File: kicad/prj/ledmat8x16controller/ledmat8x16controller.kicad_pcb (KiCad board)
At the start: 2 copper layers, 63.8 x 31.9 mm, 13 parts, among them J1 Conn_02x08_Odd_Even, J2 Conn_01x02, J3 Conn_01x02_Pin, J4 Conn_01x02_Pin, J6 Conn_01x02_Pin, J8 Conn_01x09_Pin, SW2 SW_Push

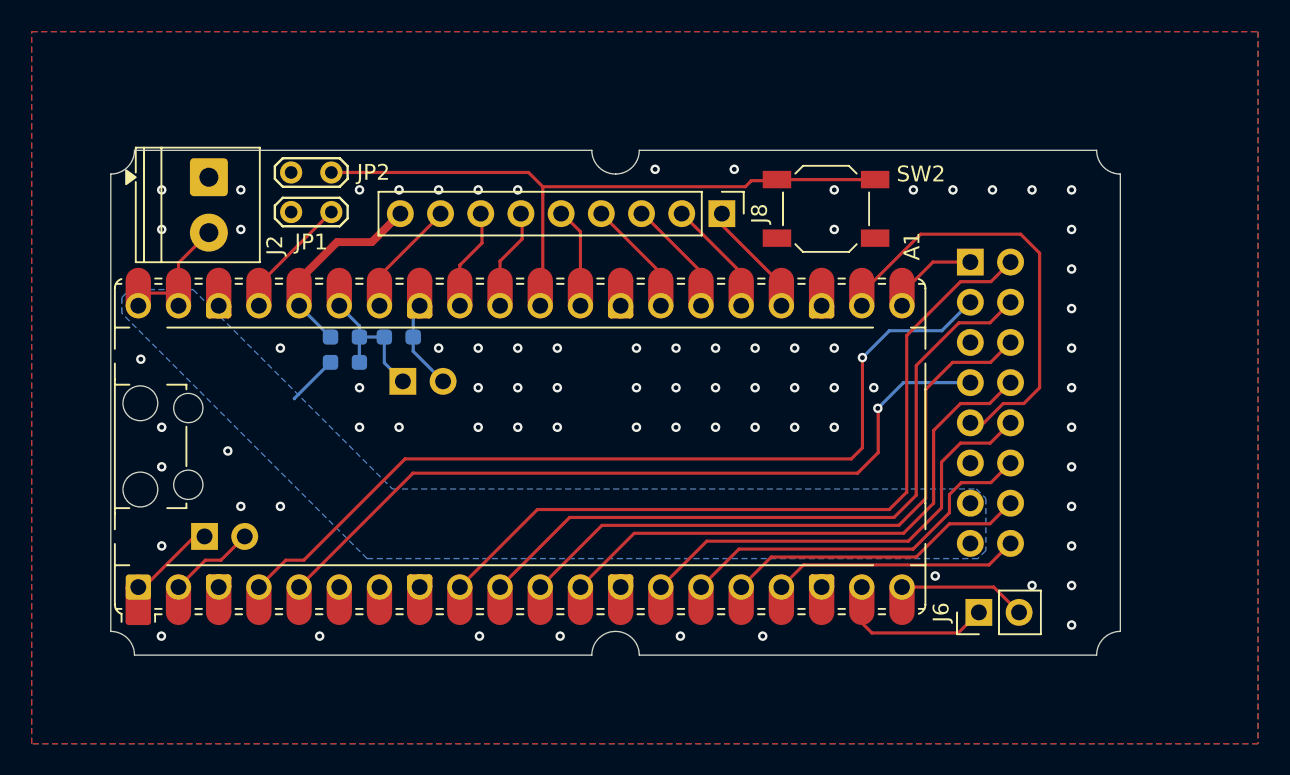
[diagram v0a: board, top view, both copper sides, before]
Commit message: Resize controller board to 32mm outline
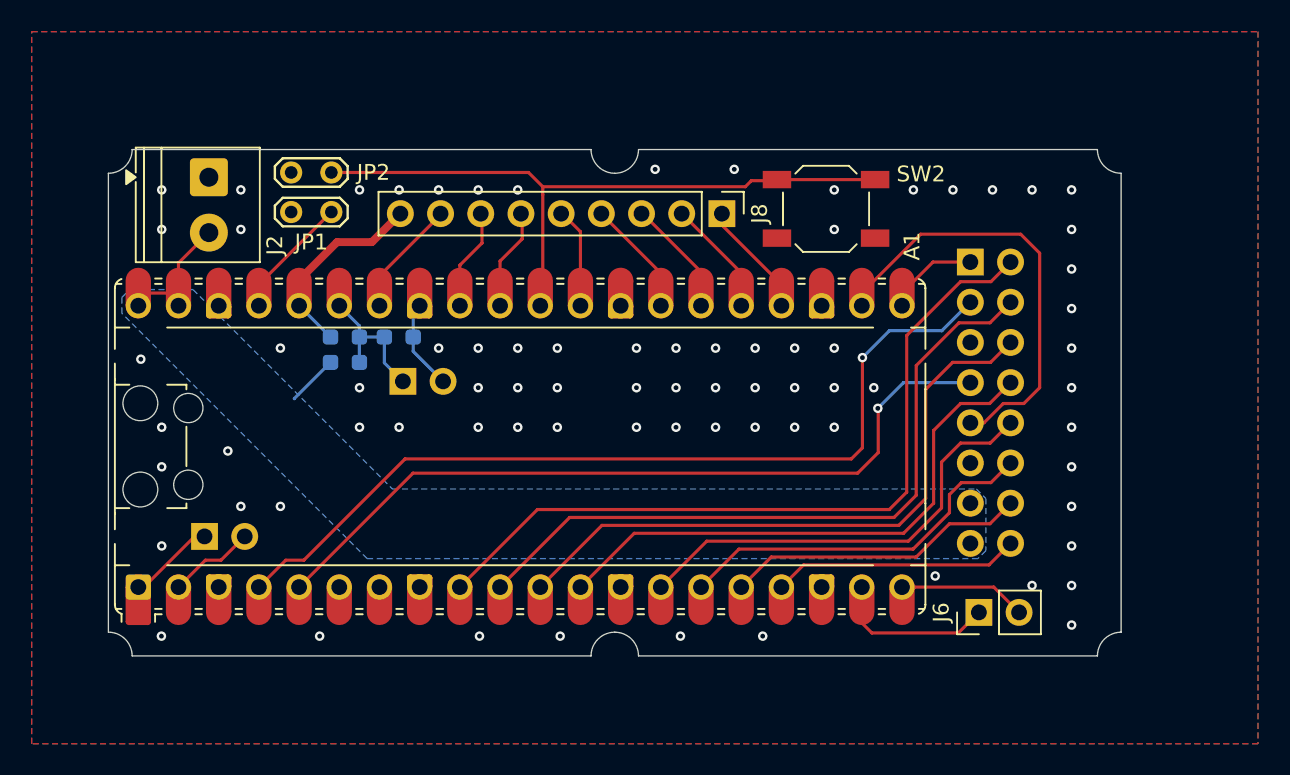
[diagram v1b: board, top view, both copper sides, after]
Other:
- board size 63.8 x 31.9 mm -> 64 x 32 mm
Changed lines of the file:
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@@
 		)
 	)
+	(property "git_hash" "Git:2eaec3c")
 	(net 0 "")
 	(net 1 "GND")
@@
 		(group ""
 			(members "0058ad3d-f0d6-4e7f-82c4-240c7e70b4a2" "00b6266a-cbbd-47b6-9ef1-1853bac25d09"
-				"104391ea-5439-40a8-8d58-6e724b40e814" "1eb92116-0edd-47a2-adbb-16db49471ecc"
-				"2a8acee5-e99d-4dde-91d9-1048e8200661" "2b792d19-000e-433a-ab8a-d0abd180f58e"
-				"3187e85b-8b3f-49bf-90ab-caa4b09ddfec" "31c9fd9d-0140-4137-93bb-e50a32028cf0"
-				"373524bd-5e5b-4e95-9ca0-5e11d2706f6d" "3996656a-93a8-4b1e-8b08-ec2c0e0e7d27"
-				"3a06dd32-a3a6-4b36-af0f-2f4e117cde2d" "3c732291-87a5-410c-b66b-d9c8d502d72e"
-				"3d1e6c50-206b-4901-bb97-596577aa74c1" "4216b5e9-156d-42f9-9ddb-c772eb940c4e"
-				"4bfd6fda-da50-4c53-b8f5-5556b6b1e2e5" "50fa3b63-8671-4821-9ecd-d2ee14772e18"
-				"5677b686-8c24-4ec1-b449-b80b724b2bba" "5bb4c3f2-826f-43f1-8862-7a750275d93b"
-				"628d2b6b-9218-437a-8487-94de9edfe95b" "658057d3-a97d-4a82-89b7-d3051213f4e8"
-				"65e31c41-0312-40f9-9e10-3a7871af7f91" "6e3fe11a-9e6b-4a0c-ad57-80ac90f94cca"
-				"744e1905-52fd-4bd7-a701-34a1fbcec512" "80ceef3d-427a-42ca-83ef-f31f25c8c388"
-				"8213ca44-72fd-4673-b862-d6101dda158a" "86a20d4a-46dc-4f83-8cc0-d4dc281a69a3"
-				"8d9d89d8-3fc2-4c28-9885-148e15c7cd48" "9485f7da-f59a-451c-964a-ce6fb43ccf66"
-				"9c866db0-bfda-407d-aabb-2fb97d60b149" "b6f4438a-0243-4b5e-9405-5ebbe4f543da"
-				"bdd1af48-56fe-47c3-b5ee-3853cbdf4550" "c03a81a3-c757-4522-93ed-0cc950156579"
-				"c0977ca8-6198-4f2c-8e10-58434674d94d" "c393c83a-7281-4ad9-870e-6dc1f0f3a5a2"
-				"ca96ae19-f84f-4d25-b0f4-7896f55b638a" "d09831e6-938e-434e-9193-577bba5c9272"
-				"d0df459c-d38e-46fd-95a1-bf1abeb8b9dc" "d14c5b17-31ab-43b7-a090-8bb9a29d612a"
-				"d1dea301-f50d-41ad-a816-984043500035" "d7ccf32c-425a-44d8-a949-7e97db540f7b"
-				"e0c28683-8850-4786-9070-989c23fdc9ee" "e15791b6-9e7a-4a08-a3b0-7906c42012af"
-				"e7a8db37-6916-418a-8dd1-057b6a85271b" "eb07a95e-324f-419d-a2db-2c45e6ab5d71"
-				"f18f225a-7b5c-4db1-bdf8-85d058df93c6" "f1d7a589-8659-4137-927e-2779f8799385"
-				"f36e8881-372f-4cab-9a68-4742cca6c638" "ff572ebc-6eb0-4867-b130-8eb4631b946b"
-			)
-		)
-		(group ""
-			(members "006b5c2c-b28d-4bce-9995-f40cade7a06c" "06221eab-dbcf-46d3-9bbb-2fd1405e9134"
-				"1509abca-39aa-4454-b6d6-1a664eebea82" "18e53b97-107d-40d0-b083-668ed06b572a"
-				"19332424-98a1-45d8-8342-42cb4fd30e7b" "1bf683cd-fbe0-4c9c-b59d-f0cd4fd6412f"
-				"2cad9b77-35cd-443b-b57c-3380c4a466cd" "388b2eac-4d35-435f-a567-fff92aa9f37d"
-				"39de895b-0006-4c25-b1a0-667f5bbee39d" "41cacaaf-efce-4e60-aece-6527953a4646"
-				"4779573b-dc70-4f3c-81f4-6778581d5189" "54ab3488-fd4e-46cd-b002-d91dd57a1ded"
-				"584b2401-7148-423a-8508-d4d69ed074ed" "5fd2c7eb-da7d-4d4b-8c2f-e0d26f77fa91"
-				"64cfef7c-a60c-48fc-9dc5-97e61f98b22a" "750995a6-9d51-4ecf-8c13-d778085f4b2d"
-				"76e7bc52-3b2a-4ecb-882e-880a05f477e7" "77589f33-3860-4c83-8974-22bdf12542ea"
-				"881e4a06-6d8f-4d12-a53d-07cff5dc1845" "98325981-72c2-48d7-9b3b-735715c64d64"
-				"9936461b-ade2-482e-85a6-48f7dcccc77c" "9a682d18-7ef6-466c-874b-ce867c586ee0"
-				"a1003cca-6dc6-4c76-be32-f5809e5d66b0" "d25d2279-7b0c-4928-bbef-4dd437ecf9ed"
-				"d4cd37cc-907e-4e48-9386-99adb3299230" "df9cc206-702e-4a70-94f9-bd8c1c5f64cf"
-				"ed96b580-88f0-45eb-9408-79810e22f87c" "f1194913-eb11-48f1-846f-3c1654de7700"
-			)
-		)
-		(group ""
-			(members "0058ad3d-f0d6-4e7f-82c4-240c7e70b4a2" "00b6266a-cbbd-47b6-9ef1-1853bac25d09"
 				"02524ea1-e8ad-46fa-b340-743d5367ed98" "104391ea-5439-40a8-8d58-6e724b40e814"
 				"15fe8b0e-d479-452a-b5dd-a1ab0046b4ec" "17a4eb0e-e9f1-4d02-abca-3baa0398bc88"
@@
 		)
 		(group ""
+			(members "006b5c2c-b28d-4bce-9995-f40cade7a06c" "06221eab-dbcf-46d3-9bbb-2fd1405e9134"
+				"1509abca-39aa-4454-b6d6-1a664eebea82" "18e53b97-107d-40d0-b083-668ed06b572a"
+				"19332424-98a1-45d8-8342-42cb4fd30e7b" "1bf683cd-fbe0-4c9c-b59d-f0cd4fd6412f"
+				"2cad9b77-35cd-443b-b57c-3380c4a466cd" "388b2eac-4d35-435f-a567-fff92aa9f37d"
+				"39de895b-0006-4c25-b1a0-667f5bbee39d" "41cacaaf-efce-4e60-aece-6527953a4646"
+				"4779573b-dc70-4f3c-81f4-6778581d5189" "54ab3488-fd4e-46cd-b002-d91dd57a1ded"
+				"584b2401-7148-423a-8508-d4d69ed074ed" "5fd2c7eb-da7d-4d4b-8c2f-e0d26f77fa91"
+				"64cfef7c-a60c-48fc-9dc5-97e61f98b22a" "750995a6-9d51-4ecf-8c13-d778085f4b2d"
+				"76e7bc52-3b2a-4ecb-882e-880a05f477e7" "77589f33-3860-4c83-8974-22bdf12542ea"
+				"881e4a06-6d8f-4d12-a53d-07cff5dc1845" "98325981-72c2-48d7-9b3b-735715c64d64"
+				"9936461b-ade2-482e-85a6-48f7dcccc77c" "9a682d18-7ef6-466c-874b-ce867c586ee0"
+				"a1003cca-6dc6-4c76-be32-f5809e5d66b0" "d25d2279-7b0c-4928-bbef-4dd437ecf9ed"
+				"d4cd37cc-907e-4e48-9386-99adb3299230" "df9cc206-702e-4a70-94f9-bd8c1c5f64cf"
+				"ed96b580-88f0-45eb-9408-79810e22f87c" "f1194913-eb11-48f1-846f-3c1654de7700"
+			)
+		)
+		(group ""
 			(members "0d40ef3d-637e-42d6-a7d9-86d2b89b3335" "4aa107e6-ed1d-44d5-a30f-b085707d9ed1"
 				"554631bd-891a-4bee-b54b-4b40b325f42f" "58812fd9-ffcb-4928-9042-52b9bd8d5f6e"
@@
 		)
 		(group ""
+			(members "4216b5e9-156d-42f9-9ddb-c772eb940c4e" "8d9d89d8-3fc2-4c28-9885-148e15c7cd48"
+				"9c866db0-bfda-407d-aabb-2fb97d60b149" "ca96ae19-f84f-4d25-b0f4-7896f55b638a"
+				"d7ccf32c-425a-44d8-a949-7e97db540f7b" "e0c28683-8850-4786-9070-989c23fdc9ee"
+				"f18f225a-7b5c-4db1-bdf8-85d058df93c6" "f1d7a589-8659-4137-927e-2779f8799385"
+			)
+		)
+		(group ""
 			(members "0005767a-353b-4003-bab9-c37b381233bd" "059b6c05-2a2f-4295-a877-caf2a8b81714"
 				"13d216e6-ed68-40dd-9f70-11fc93da3dc8" "168faab2-408d-4c40-bd02-b4aaa10ba6fb"
@@
 	)
 	(gr_arc
-		(start 127 55.7)
-		(mid 126.56066 56.76066)
-		(end 125.5 57.2)
+		(start 158.85 55.649999)
+		(mid 158.410661 56.71066)
+		(end 157.35 57.149999)
 		(stroke
 			(width 0.05)
@@
 	)
 	(gr_line
-		(start 187.8 87.6)
-		(end 158.9 87.6)
+		(start 125.35 86.149999)
+		(end 125.35 57.149999)
 		(stroke
 			(width 0.05)
@@
 		(layer "Edge.Cuts")
 	)
-	(gr_line
-		(start 158.9 55.7)
-		(end 187.8 55.7)
+	(gr_arc
+		(start 157.349998 57.149999)
+		(mid 156.289339 56.710658)
+		(end 155.849998 55.649999)
 		(stroke
 			(width 0.05)
@@
 		(layer "Edge.Cuts")
 	)
-	(gr_arc
-		(start 157.4 57.2)
-		(mid 156.33934 56.76066)
-		(end 155.9 55.7)
+	(gr_line
+		(start 187.85 55.649999)
+		(end 158.85 55.649999)
 		(stroke
 			(width 0.05)
@@
 		(layer "Edge.Cuts")
 	)
-	(gr_arc
-		(start 125.5 86.1)
-		(mid 126.56066 86.53934)
-		(end 127 87.6)
+	(gr_line
+		(start 155.85 87.649999)
+		(end 126.85 87.649999)
 		(stroke
 			(width 0.05)
@@
 	)
 	(gr_arc
-		(start 187.8 87.6)
-		(mid 188.23934 86.53934)
-		(end 189.3 86.1)
+		(start 126.85 55.649999)
+		(mid 126.410661 56.71066)
+		(end 125.35 57.149999)
 		(stroke
 			(width 0.05)
@@
 	)
 	(gr_line
-		(start 155.9 87.6)
-		(end 127 87.6)
+		(start 187.85 87.649999)
+		(end 158.85 87.649999)
 		(stroke
 			(width 0.05)
@@
 		(layer "Edge.Cuts")
 	)
-	(gr_line
-		(start 125.5 86.1)
-		(end 125.5 57.2)
+	(gr_arc
+		(start 155.849999 87.649998)
+		(mid 156.289339 86.589339)
+		(end 157.349999 86.149998)
 		(stroke
 			(width 0.05)
@@
 	)
 	(gr_arc
-		(start 189.3 57.2)
-		(mid 188.23934 56.76066)
-		(end 187.8 55.7)
+		(start 189.35 57.149999)
+		(mid 188.28934 56.710659)
+		(end 187.85 55.649999)
 		(stroke
 			(width 0.05)
@@
 	)
 	(gr_arc
-		(start 157.4 86.1)
-		(mid 158.46066 86.53934)
-		(end 158.9 87.6)
+		(start 125.35 86.149999)
+		(mid 126.410661 86.589339)
+		(end 126.85 87.649999)
 		(stroke
 			(width 0.05)
@@
 		(layer "Edge.Cuts")
 	)
-	(gr_arc
-		(start 158.9 55.7)
-		(mid 158.46066 56.76066)
-		(end 157.4 57.2)
+	(gr_line
+		(start 189.35 57.149999)
+		(end 189.35 86.149999)
 		(stroke
 			(width 0.05)
@@
 	)
 	(gr_line
-		(start 127 55.7)
-		(end 155.9 55.7)
+		(start 155.85 55.649999)
+		(end 126.85 55.649999)
 		(stroke
 			(width 0.05)
@@
 	)
 	(gr_arc
-		(start 155.9 87.6)
-		(mid 156.33934 86.53934)
-		(end 157.4 86.1)
+		(start 157.35 86.149999)
+		(mid 158.410661 86.589339)
+		(end 158.85 87.649999)
 		(stroke
 			(width 0.05)
@@
 		(layer "Edge.Cuts")
 	)
-	(gr_line
-		(start 189.3 57.2)
-		(end 189.3 86.1)
+	(gr_arc
+		(start 187.85 87.649999)
+		(mid 188.28934 86.589339)
+		(end 189.35 86.149999)
 		(stroke
 			(width 0.05)

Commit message: Add missing git hash silkscreen to controller board
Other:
- board text added: "${git_hash}"
- board text added: "github.com/burbschat/ledmat8x16"
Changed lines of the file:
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@@
 		(layer "Edge.Cuts")
+	)
+	(gr_text "github.com/burbschat/ledmat8x16"
+		(at 161.5 80.699999 0)
+		(layer "B.SilkS")
+		(effects
+			(font
+				(size 1 1)
+				(thickness 0.15)
+			)
+			(justify bottom mirror)
+		)
+	)
+	(gr_text "${git_hash}"
+		(at 161.5 78.699999 0)
+		(layer "B.SilkS")
+		(effects
+			(font
+				(size 1 1)
+				(thickness 0.15)
+			)
+			(justify bottom mirror)
+		)
 	)
 	(via

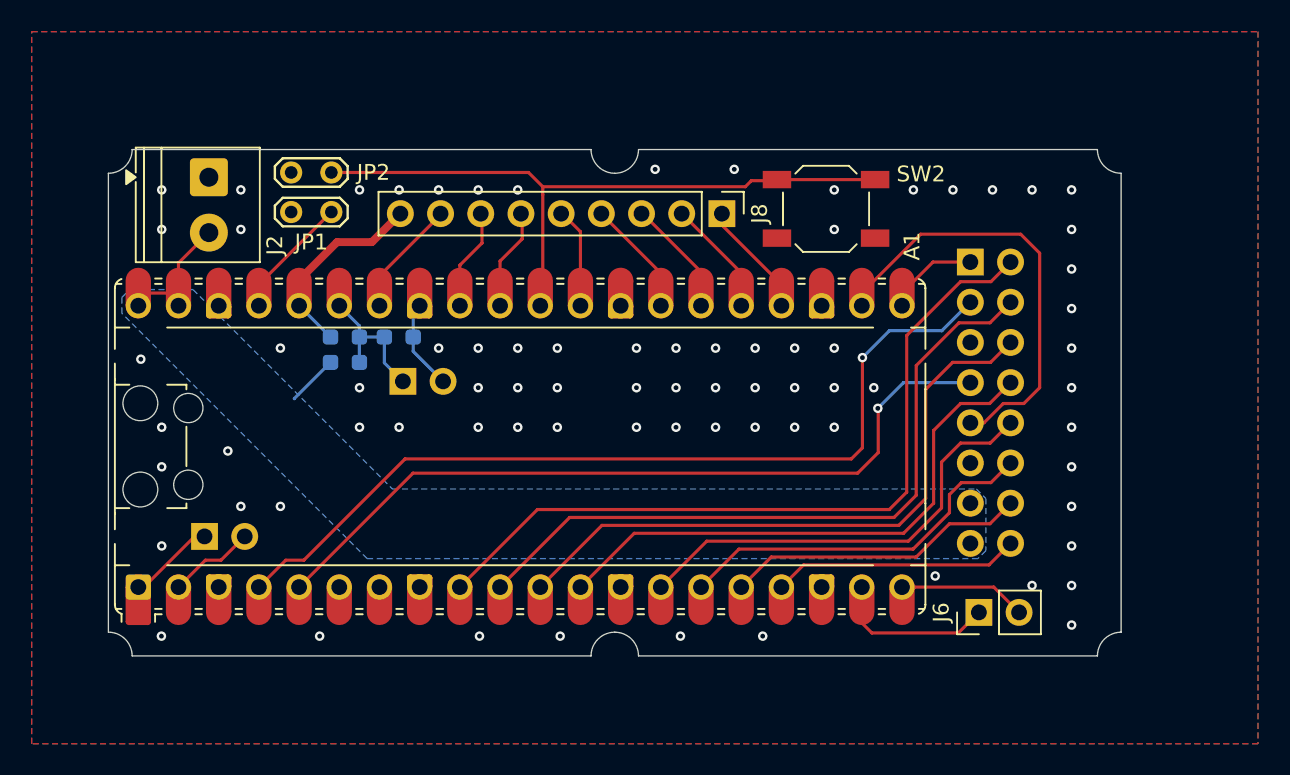
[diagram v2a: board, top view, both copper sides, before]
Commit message: Rework the controller (pico carrier) board
Previous version was thrown together in a short time as I was ordering
boards anyways and wanted to test the concept for a pico carrier thing.
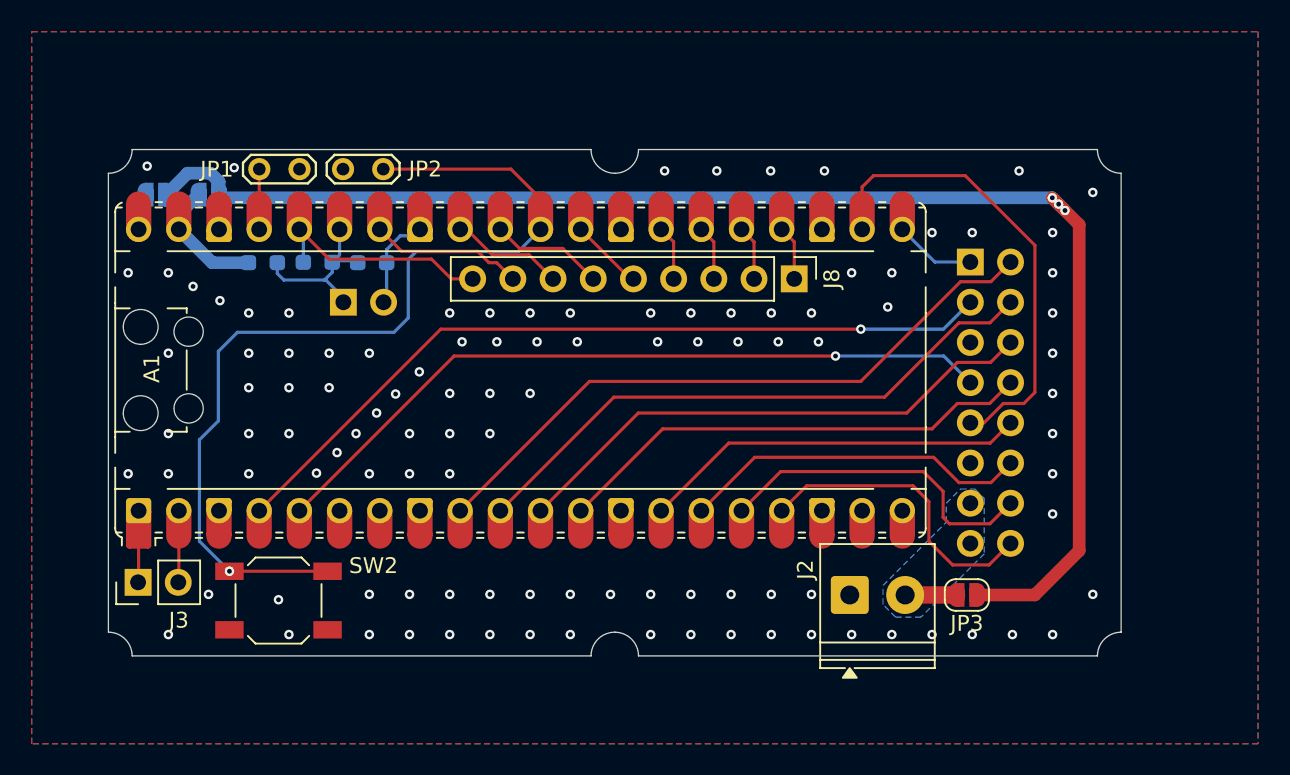
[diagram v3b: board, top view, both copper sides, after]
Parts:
- removed J6: Conn_01x02_Pin, Connector_PinHeader_2.54mm:PinHeader_1x02_P2.54mm_Vertical
- added JP3: Jumper_2_Open, Jumper:SolderJumper-2_P1.3mm_Open_RoundedPad1.0x1.5mm, F.Cu at (179.6, 83.8)
- added JP4: Jumper_2_Open, Jumper:SolderJumper-2_P1.3mm_Open_RoundedPad1.0x1.5mm, B.Cu at (131.7, 58.5)
- added JP5: Jumper_2_Open, Jumper:SolderJumper-2_P1.3mm_Open_RoundedPad1.0x1.5mm, B.Cu at (128.3, 58.5)
- J3: moved to F.Cu
- moved J2 48.3 mm to (172.2, 83.8), turned to 0 degrees
- moved SW2 42.5 mm to (136.1, 84.1)
- moved R1 8.16 mm to (135.1, 62.8)
- moved J4 6.26 mm to (140.2, 65.3)
- moved J8 6.16 mm to (168.7, 63.8)
- moved J3 5.10 mm to (127.2, 83.0), turned to 90 degrees
- moved R2 5.03 mm to (138.6, 62.8)
- moved R3 4.99 mm to (142.0, 62.8)
- moved A1 4.83 mm to (151.4, 69.6)
- moved JP2 3.28 mm to (140.2, 56.9)
- moved JP1 2.76 mm to (137.4, 56.9), turned to 180 degrees
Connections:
- net /GPIO5 renamed /GPIO5_1
- A1 pad 19: /GPIO14 -> /GPIO14_1
- A1 pad 20: /GPIO15 -> /GPIO15_1
- A1 pad 39: +5V -> /VSYS
- A1 pad 40: +5V -> /VBUS
- J1 pad 13: +5V -> +5V_EXT
- J1 pad 15: +5V -> +5V_EXT
- J2 pad 2: +5V -> +5V_EXT
- R1 pad 1: +5V -> /VSYS
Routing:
- net /POWER_BUS: track 0.00 -> 89.4 mm, vias 0 -> 3
- net /MCU_RESET: track 41.7 -> 59.0 mm, vias 0 -> 1
- net +5V: track 10.4 -> 0.00 mm
- net /GPIO14: track 9.66 -> 0.00 mm
- net /GPIO15: track 8.39 -> 0.00 mm
- net /VSYS: track 0.00 -> 7.98 mm
- net /ROW8: track 49.1 -> 41.3 mm
- net /ROW7: track 44.5 -> 37.7 mm
- net /ROW6: track 40.2 -> 34.1 mm
- net /SOUT: track 55.8 -> 50.4 mm
- net /ROW5: track 35.2 -> 30.5 mm
- net /ROW4: track 28.1 -> 24.4 mm
- net /ROW1: track 15.6 -> 19.2 mm
- net +5V_EXT: track 0.00 -> 3.25 mm
- net /PICO_RESET: track 7.02 -> 3.82 mm
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- added copper zone on B.Cu, net +5V_EXT
- removed copper zone on B.Cu, net +5V

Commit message: Additions to silkscreen
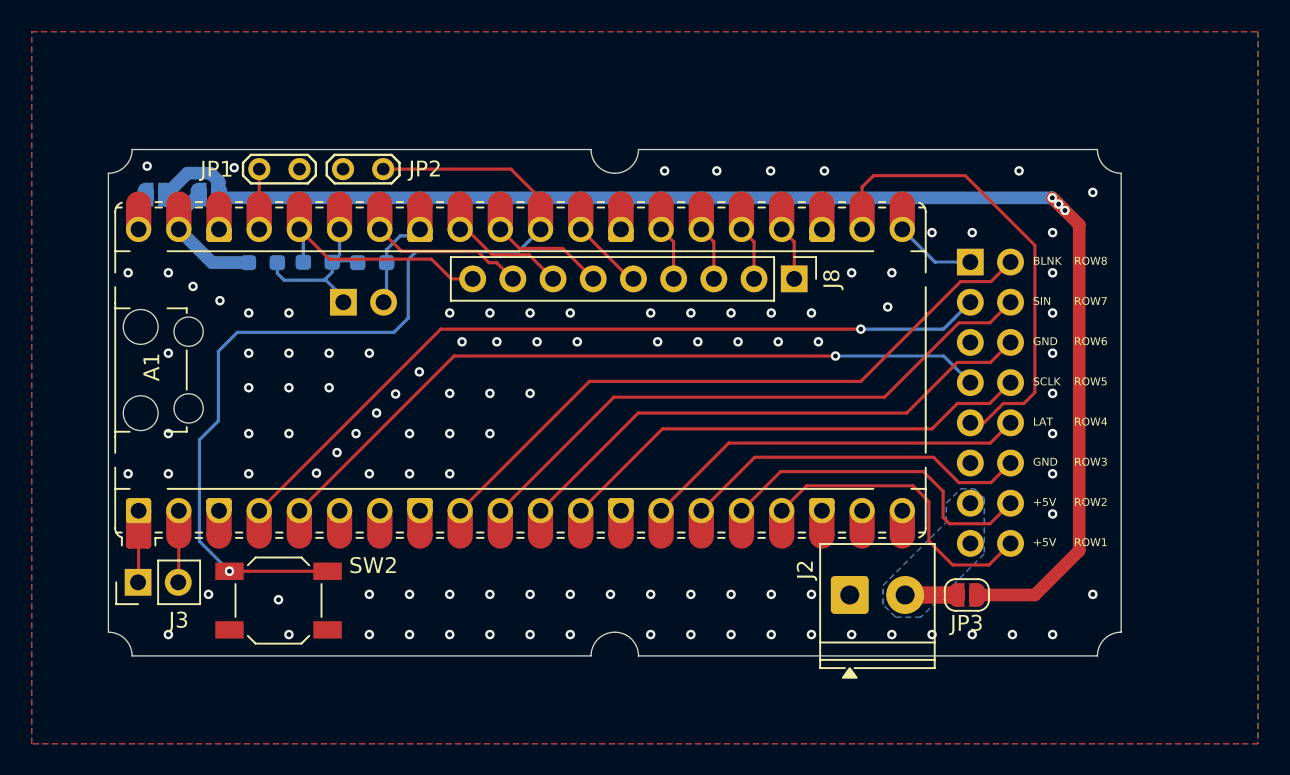
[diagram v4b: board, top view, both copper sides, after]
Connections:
- net /GPIO14_1 renamed /GPIO14
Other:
- board text added: "+5V"
- board text added: "BLNK"
- board text added: "GND"
- board text added: "LAT"
- board text added: "ROW1"
- board text added: "ROW2"
- board text added: "ROW3"
- board text added: "ROW4"
- board text added: "ROW5"
- board text added: "ROW6"
- board text added: "ROW7"
- board text added: "ROW8"
- board text added: "SCLK"
- board text added: "SIN"
